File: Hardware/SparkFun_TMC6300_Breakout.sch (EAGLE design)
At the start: 34 parts, among them U2 TMC6300

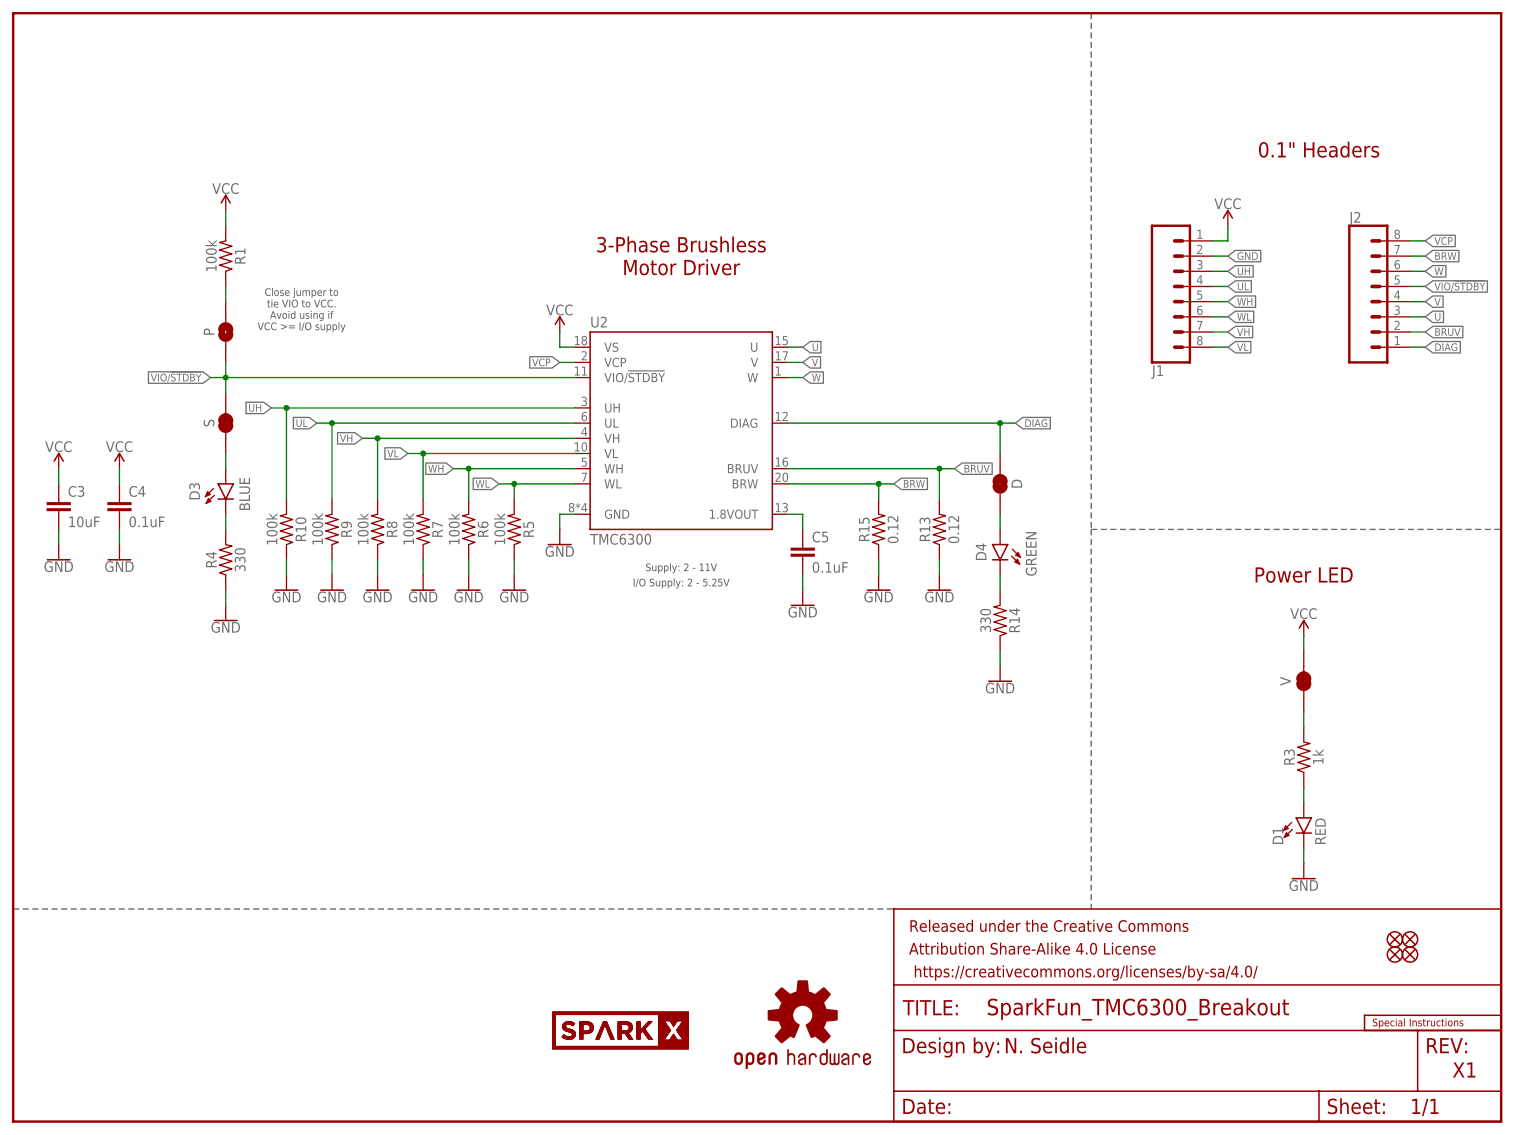
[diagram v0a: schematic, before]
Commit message: Fix pinout to emulate other reprap style drivers
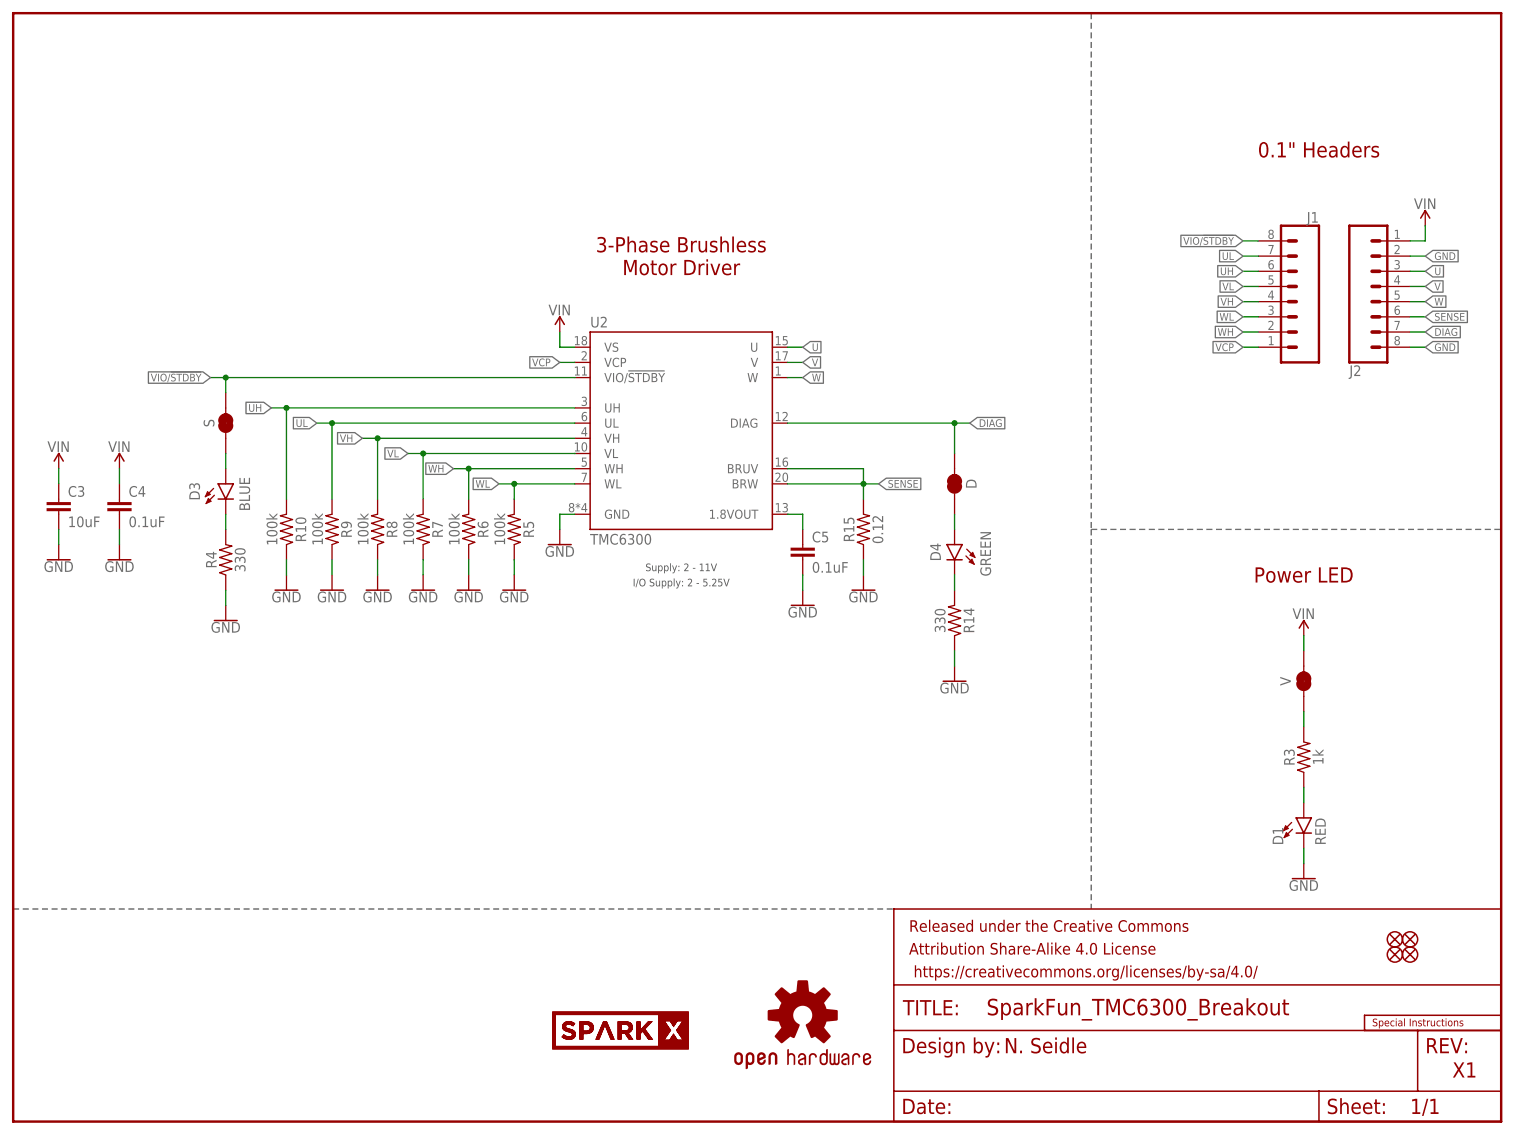
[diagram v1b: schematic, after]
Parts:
- removed P: JUMPER-SMT_2_NO_SILK, SparkFun-Jumpers:JUMPER-SMT_2_NO_SILK
- removed R1: 100k, SparkFun-Resistors:100KOHM-0603-1/10W-1%
- removed R13: 0.12, SparkFun-Resistors:0.12OHM-1206-1/2W-1%
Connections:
- removed net BRUV: J2.2, R13.2, U2.BRUV
- removed net BRW: J2.7, R15.2, U2.BRW
- removed net N$2: P.2, R1.1
- removed net VCC: C3.1, C4.1, J1.1, R1.2, U2.VS, V.2
- new net SENSE: J2.6, R15.2, U2.BRUV, U2.BRW
- new net VIN: C3.1, C4.1, J2.1, U2.VS, V.2
- net DIAG: now also J2.7; no longer J2.1
- net GND: now also J2.2, J2.8; no longer J1.2, R13.1
- net UH: now also J1.6; no longer J1.3
- net UL: now also J1.7; no longer J1.4
- net VCP: now also J1.1; no longer J2.8
- net VH: now also J1.4; no longer J1.7
- net VIO/!STDBY!: now also J1.8; no longer J2.5, P.1
- net VL: now also J1.5; no longer J1.8
- net W: now also J2.5; no longer J2.6
- net WH: now also J1.2; no longer J1.5
- net WL: now also J1.3; no longer J1.6
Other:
- note removed: "Close jumper to tie VIO to VCC. Avoid using if VCC >= I/O supply"
- moved on the sheet: D, D4, J1, J2, R14, R15
